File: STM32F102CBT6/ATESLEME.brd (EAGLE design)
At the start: 35.3 x 57.9 mm, 55 parts, among them U1 ADXL345PATRICK, U3 AMS1117-3.3, U4 STM32F102CBT6, Y2 ABM2B-8.000MHZ-10-1-U-T

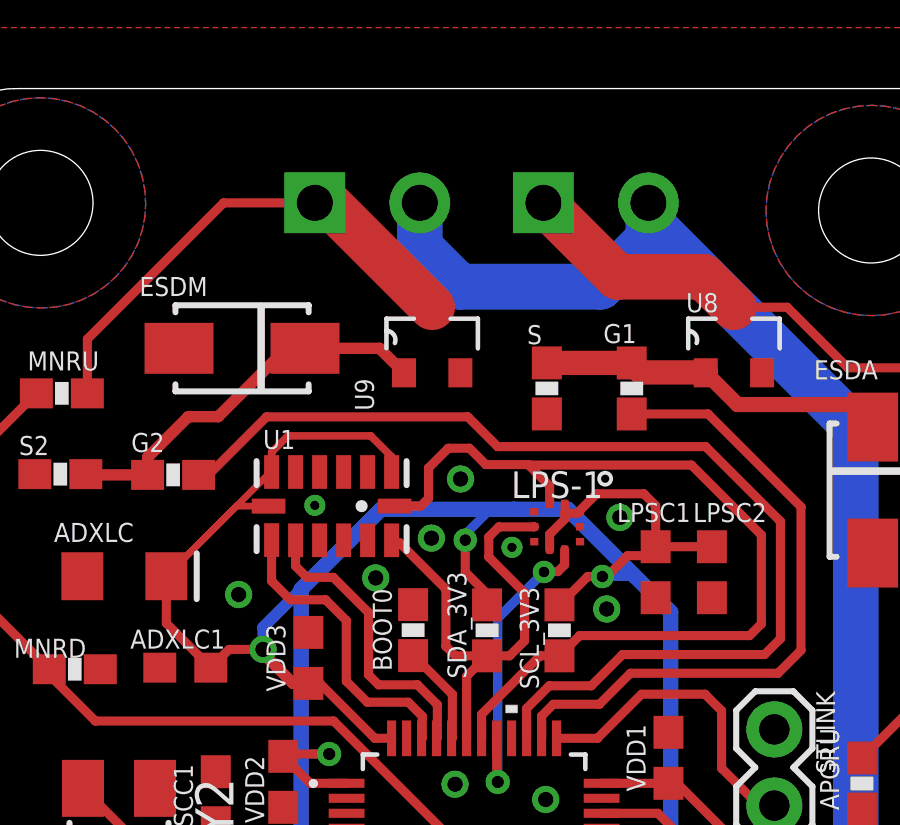
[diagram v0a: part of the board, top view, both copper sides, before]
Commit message: Polygon 15 mils
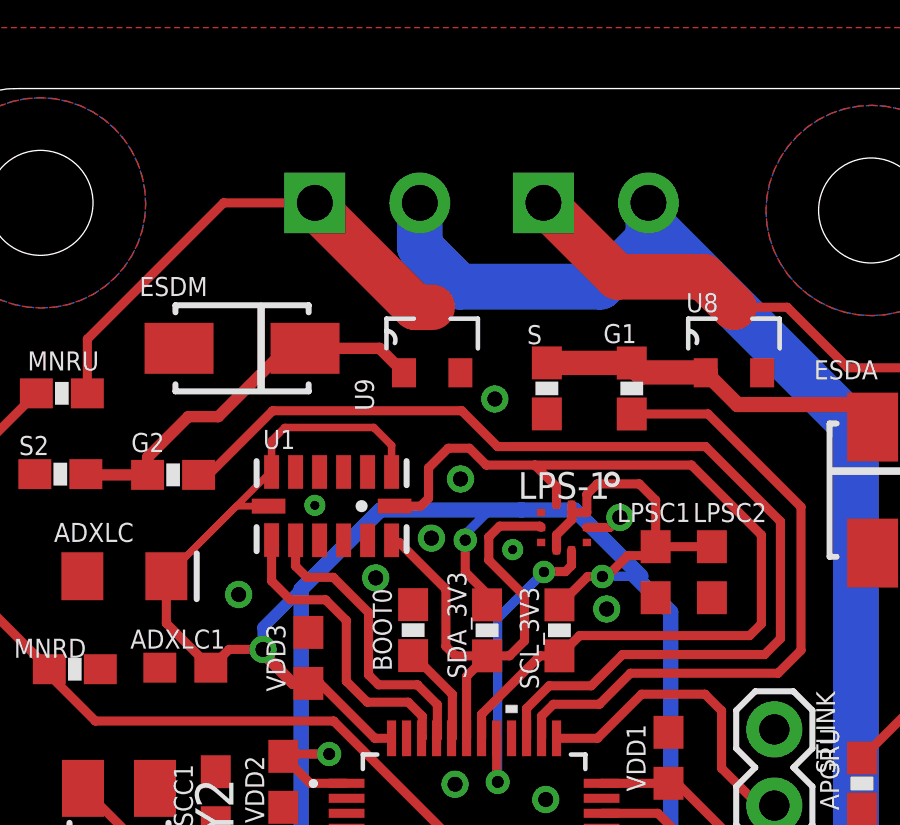
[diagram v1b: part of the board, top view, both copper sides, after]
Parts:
- moved LPS-1 0.23 mm to (15.1, 49.7)
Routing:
- net 3.3V: track 140.2 -> 142.0 mm
- net GND: track 0.00 -> 1.24 mm, vias 10 -> 11
